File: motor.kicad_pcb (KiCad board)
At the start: 2 copper layers, 100 x 100 mm, 74 parts, among them J1 Gates_B, J2 PWM_B, J3 I2C, J41 Jump_ID_A, J43 ATX_power, J46 Fan_vol_sel, J48 Power_male, J49 Power_female, J50 Power_signal_male, J51 Power_signal_female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

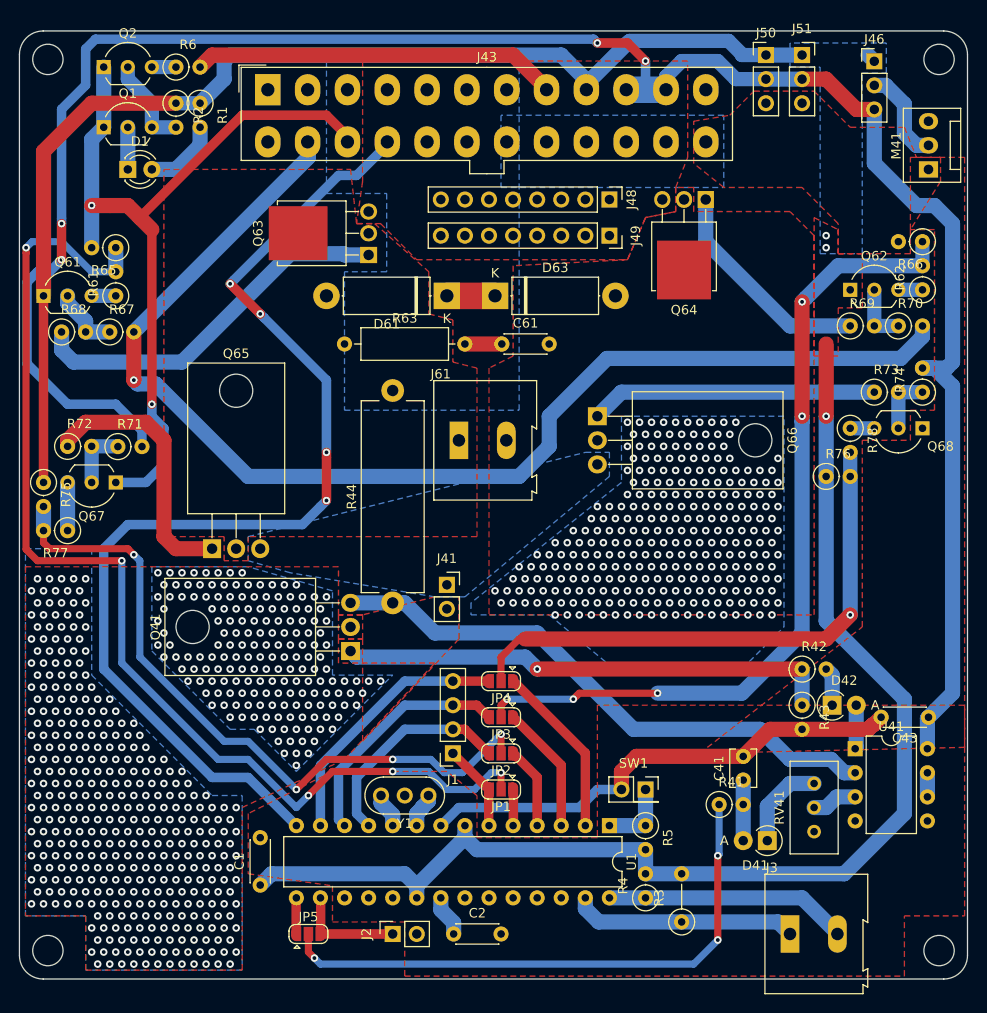
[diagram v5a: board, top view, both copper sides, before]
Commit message: PCB: Add/move silks
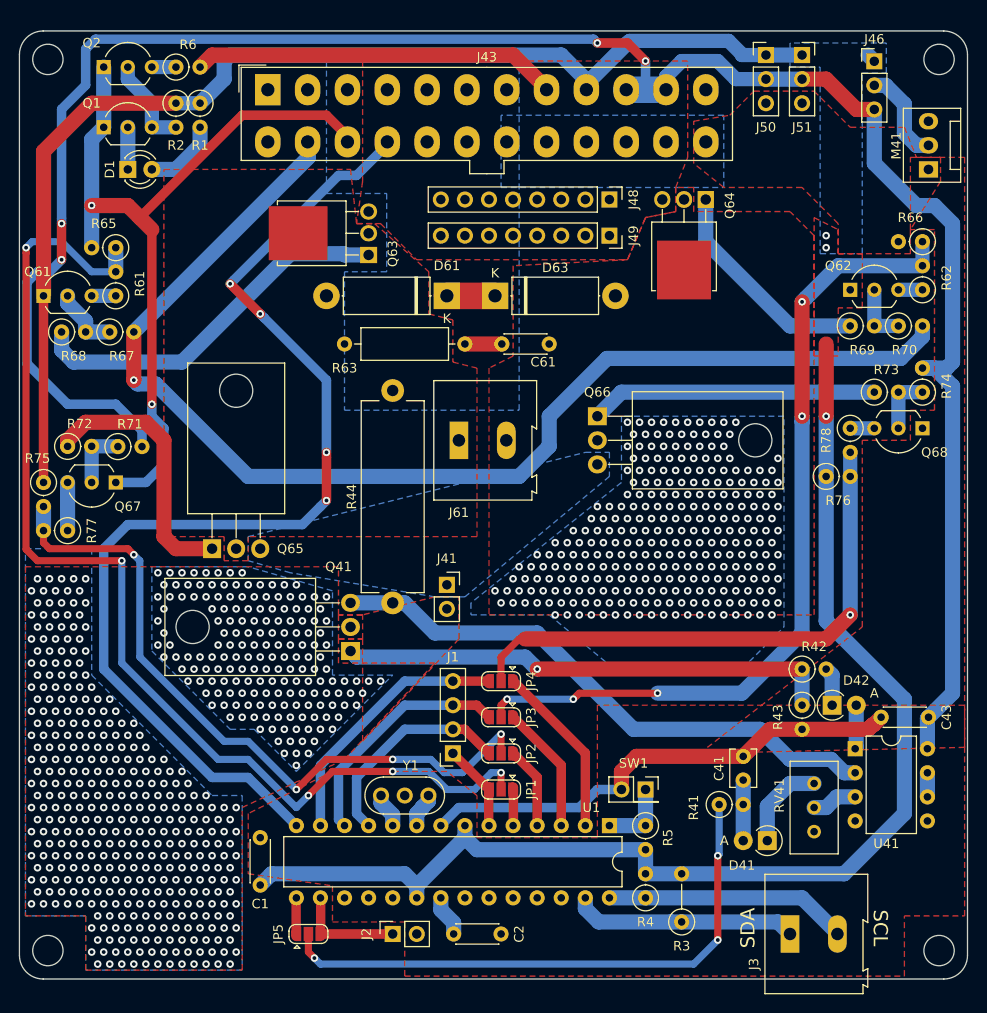
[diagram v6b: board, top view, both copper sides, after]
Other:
- board text added: "SCL"
- board text added: "SDA"
